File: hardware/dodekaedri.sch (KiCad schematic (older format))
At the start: 0 parts

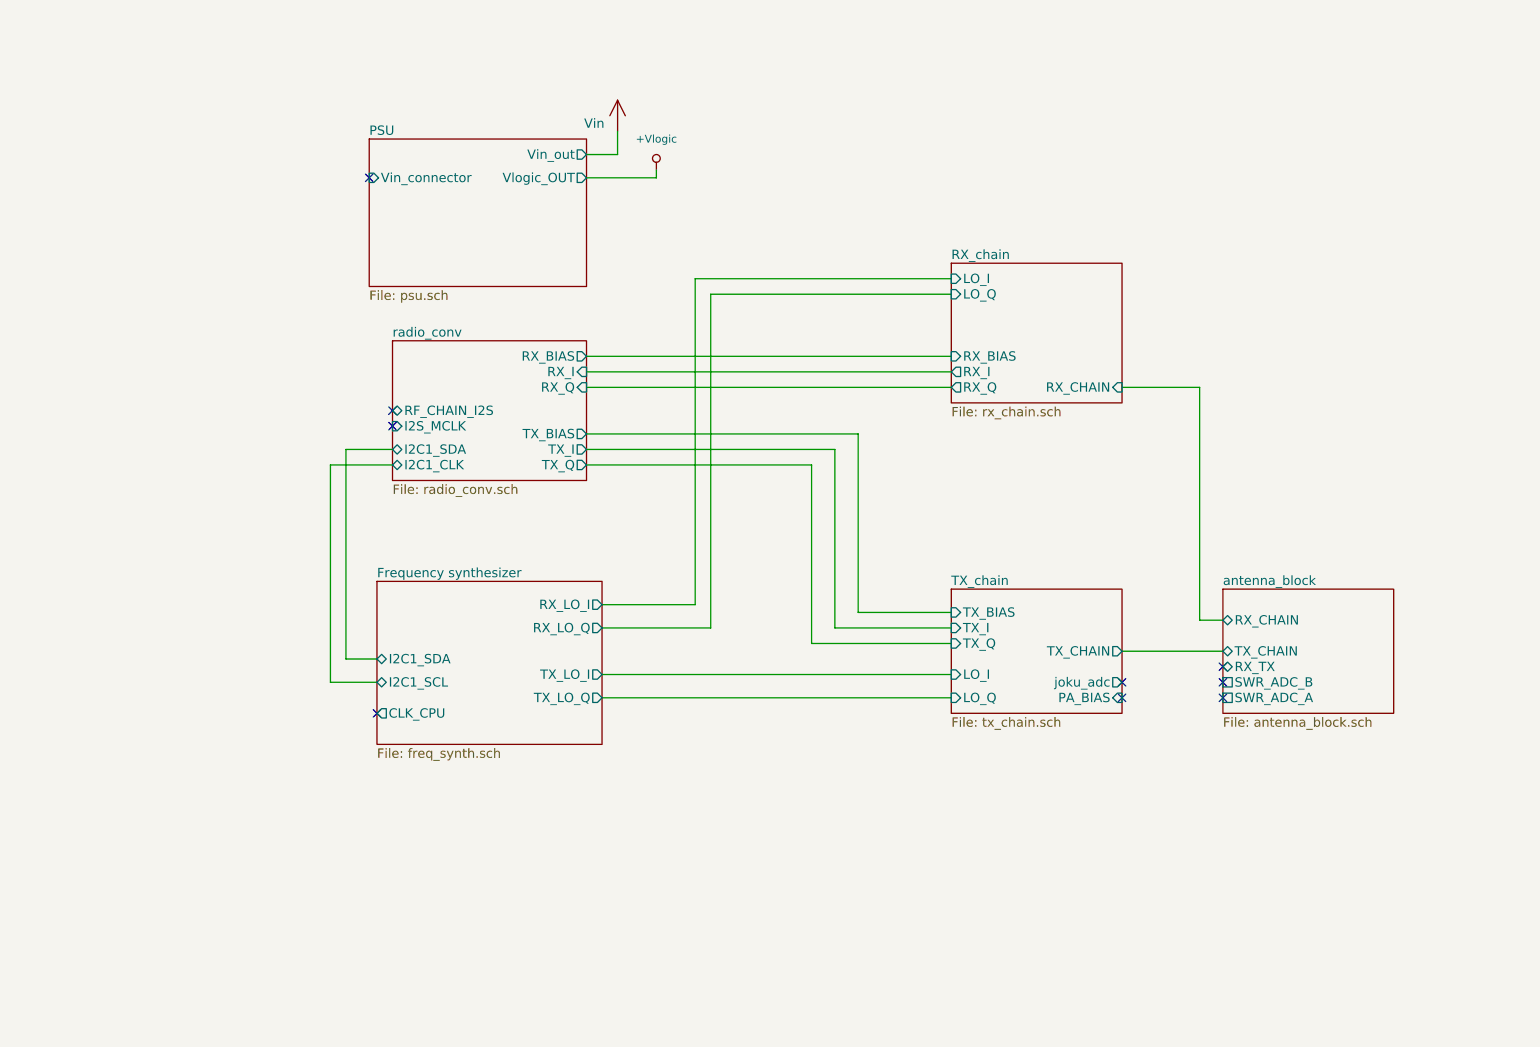
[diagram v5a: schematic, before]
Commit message: Added initial CPU block and fixed bugs from other sheets
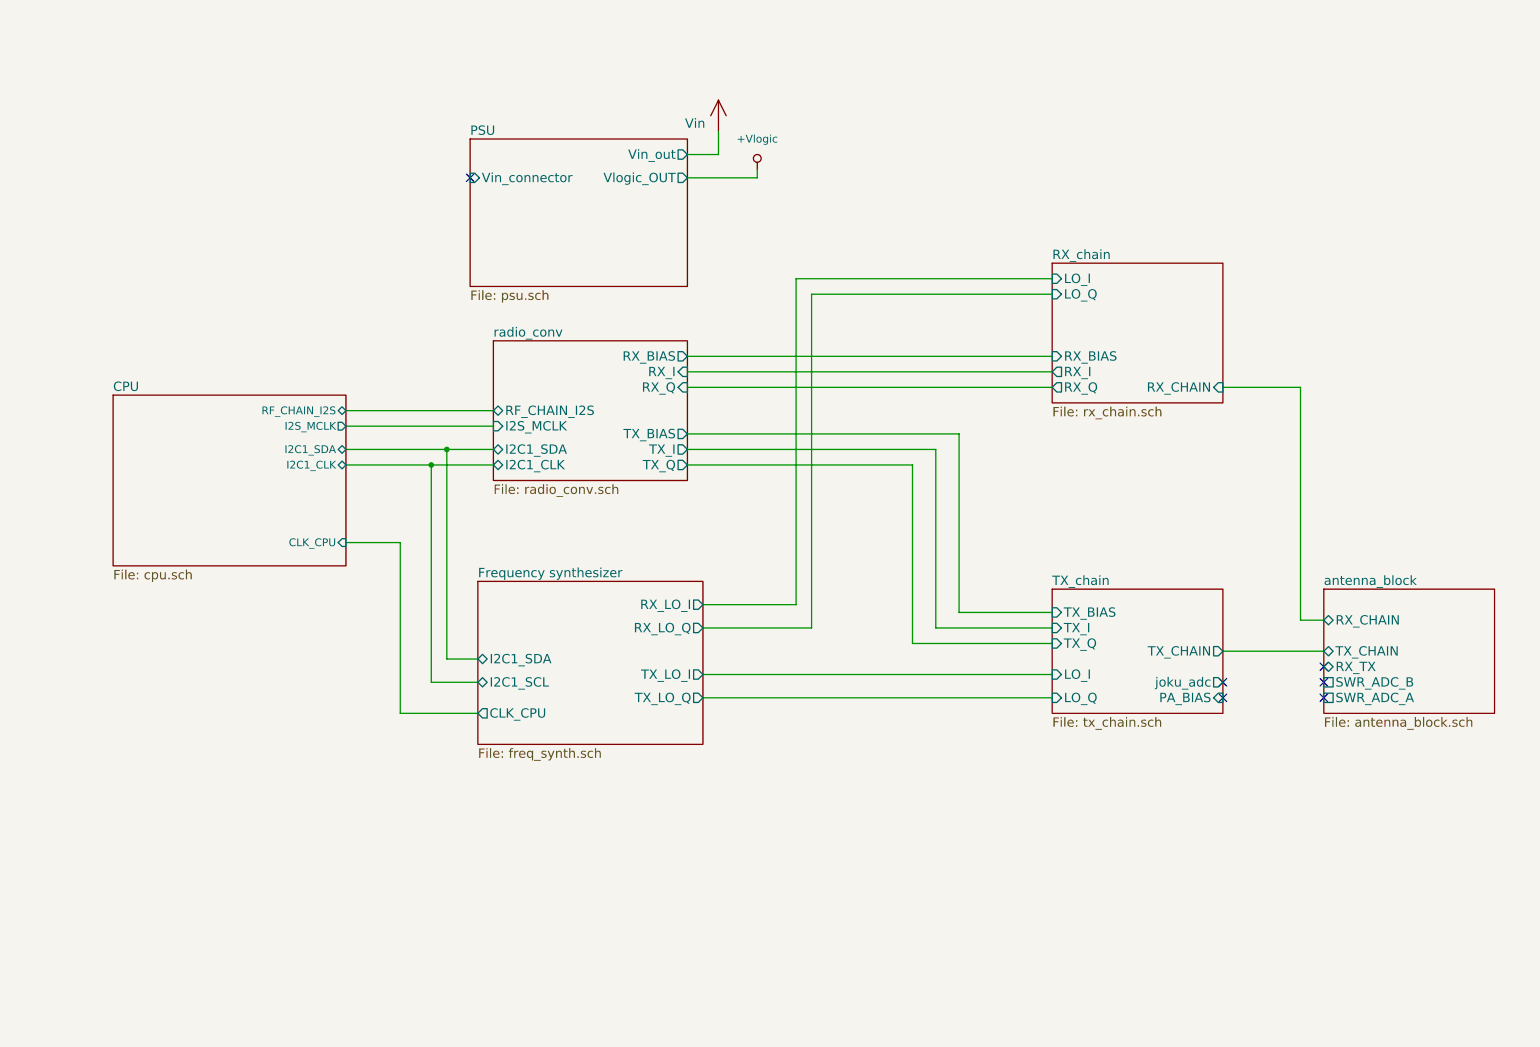
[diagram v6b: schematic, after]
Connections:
- no-connect marks 9 -> 6
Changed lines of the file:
@@
 LIBS:dodekaedri
 LIBS:Oscillators
+LIBS:stm32
 LIBS:dodekaedri-cache
 EELAYER 25 0
@@
 $Descr A4 11693 8268
 encoding utf-8
-Sheet 1 7
+Sheet 1 8
 Title "Block layer"
 Date "2016-09-20"
-Rev "0.1"
+Rev "0.4"
 Comp "PRK - OH2TI"
 Comment1 "exla - OH2EHK"
@@
 $EndDescr
 $Sheet
-S 3200 4550 1450 1050
+S 3850 4550 1450 1050
 U 57E30E5C
 F0 "Frequency synthesizer" 60
 F1 "freq_synth.sch" 60
-F2 "CLK_CPU" O L 3200 5400 60
-F3 "I2C1_SCL" B L 3200 5200 60
-F4 "I2C1_SDA" B L 3200 5050 60
-F5 "TX_LO_I" O R 4650 5150 60
-F6 "TX_LO_Q" O R 4650 5300 60
-F7 "RX_LO_Q" O R 4650 4850 60
-F8 "RX_LO_I" O R 4650 4700 60
-$EndSheet
-$Sheet
-S 8650 4600 1100 800
+F2 "CLK_CPU" O L 3850 5400 60
+F3 "I2C1_SCL" B L 3850 5200 60
+F4 "I2C1_SDA" B L 3850 5050 60
+F5 "TX_LO_I" O R 5300 5150 60
+F6 "TX_LO_Q" O R 5300 5300 60
+F7 "RX_LO_Q" O R 5300 4850 60
+F8 "RX_LO_I" O R 5300 4700 60
+$EndSheet
+$Sheet
+S 9300 4600 1100 800
 U 57E31F2A
 F0 "antenna_block" 60
 F1 "antenna_block.sch" 60
-F2 "SWR_ADC_A" U L 8650 5300 60
-F3 "SWR_ADC_B" U L 8650 5200 60
-F4 "TX_CHAIN" B L 8650 5000 60
-F5 "RX_TX" B L 8650 5100 60
-F6 "RX_CHAIN" B L 8650 4800 60
-$EndSheet
-$Sheet
-S 3150 1700 1400 950
+F2 "SWR_ADC_A" U L 9300 5300 60
+F3 "SWR_ADC_B" U L 9300 5200 60
+F4 "TX_CHAIN" B L 9300 5000 60
+F5 "RX_TX" B L 9300 5100 60
+F6 "RX_CHAIN" B L 9300 4800 60
+$EndSheet
+$Sheet
+S 3800 1700 1400 950
 U 57E31551
 F0 "PSU" 60
 F1 "psu.sch" 60
-F2 "Vlogic_OUT" O R 4550 1950 60
-F3 "Vin_connector" I L 3150 1950 60
-F4 "Vin_out" O R 4550 1800 60
+F2 "Vlogic_OUT" O R 5200 1950 60
+F3 "Vin_connector" I L 3800 1950 60
+F4 "Vin_out" O R 5200 1800 60
 $EndSheet
 $Comp
 L +Vlogic #PWR01
 U 1 1 57E3367B
-P 5000 1900
-F 0 "#PWR01" H 5000 1700 50  0001 C CNN
-F 1 "+Vlogic" H 5000 2100 50  0000 C CNN
-F 2 "" H 5000 1900 50  0000 C CNN
-F 3 "" H 5000 1900 50  0000 C CNN
-	1    5000 1900
+P 5650 1900
+F 0 "#PWR01" H 5650 1700 50  0001 C CNN
+F 1 "+Vlogic" H 5650 2100 50  0000 C CNN
+F 2 "" H 5650 1900 50  0000 C CNN
+F 3 "" H 5650 1900 50  0000 C CNN
+	1    5650 1900
 	1    0    0    -1
 $EndComp
 $Sheet
-S 6900 4600 1100 800
+S 7550 4600 1100 800
 U 57E42B3F
 F0 "TX_chain" 60
 F1 "tx_chain.sch" 60
-F2 "TX_I" I L 6900 4850 60
-F3 "TX_Q" I L 6900 4950 60
-F4 "LO_I" I L 6900 5150 60
-F5 "LO_Q" I L 6900 5300 60
-F6 "PA_BIAS" I R 8000 5300 60
-F7 "TX_CHAIN" O R 8000 5000 60
-F8 "joku_adc" O R 8000 5200 60
-F9 "TX_BIAS" I L 6900 4750 60
-$EndSheet
-NoConn ~ 3200 5400
-NoConn ~ 8000 5200
-NoConn ~ 8000 5300
-NoConn ~ 8650 5100
+F2 "TX_I" I L 7550 4850 60
+F3 "TX_Q" I L 7550 4950 60
+F4 "LO_I" I L 7550 5150 60
+F5 "LO_Q" I L 7550 5300 60
+F6 "PA_BIAS" I R 8650 5300 60
+F7 "TX_CHAIN" O R 8650 5000 60
+F8 "joku_adc" O R 8650 5200 60
+F9 "TX_BIAS" I L 7550 4750 60
+$EndSheet
 NoConn ~ 8650 5200
 NoConn ~ 8650 5300
-$Sheet
-S 6900 2500 1100 900
+NoConn ~ 9300 5100
+NoConn ~ 9300 5200
+NoConn ~ 9300 5300
+$Sheet
+S 7550 2500 1100 900
 U 57E4503B
 F0 "RX_chain" 60
 F1 "rx_chain.sch" 60
-F2 "RX_CHAIN" I R 8000 3300 60
-F3 "LO_I" I L 6900 2600 60
-F4 "LO_Q" I L 6900 2700 60
-F5 "RX_I" O L 6900 3200 60
-F6 "RX_Q" O L 6900 3300 60
-F7 "RX_BIAS" I L 6900 3100 60
-$EndSheet
-Wire Wire Line
-	4550 1950 5000 1950
-Wire Wire Line
-	5000 1950 5000 1900
-Wire Wire Line
-	6150 4850 6900 4850
-Wire Wire Line
-	6000 4950 6900 4950
-Wire Wire Line
-	4650 5150 6900 5150
-Wire Wire Line
-	4650 5300 6900 5300
-Wire Wire Line
-	8000 5000 8650 5000
-Wire Wire Line
-	4550 3800 6000 3800
-Wire Wire Line
-	6000 3800 6000 4950
-Wire Wire Line
-	6150 4850 6150 3700
-Wire Wire Line
-	6150 3700 4550 3700
-Wire Wire Line
-	3300 3700 3000 3700
-Wire Wire Line
-	3000 3700 3000 5050
-Wire Wire Line
-	3000 5050 3200 5050
-Wire Wire Line
-	3300 3800 2900 3800
-Wire Wire Line
-	2900 3800 2900 5200
-Wire Wire Line
-	2900 5200 3200 5200
-Wire Wire Line
-	5250 2600 6900 2600
-Wire Wire Line
-	5350 2700 6900 2700
-Wire Wire Line
-	8000 3300 8500 3300
-Wire Wire Line
-	8500 3300 8500 4800
-Wire Wire Line
-	8500 4800 8650 4800
-Wire Wire Line
-	4550 3200 6900 3200
-Wire Wire Line
-	4550 3300 6900 3300
-Wire Wire Line
-	4650 4700 5250 4700
-Wire Wire Line
-	5250 4700 5250 2600
-Wire Wire Line
-	5350 2700 5350 4850
-Wire Wire Line
-	5350 4850 4650 4850
-NoConn ~ 3150 1950
+F2 "RX_CHAIN" I R 8650 3300 60
+F3 "LO_I" I L 7550 2600 60
+F4 "LO_Q" I L 7550 2700 60
+F5 "RX_I" O L 7550 3200 60
+F6 "RX_Q" O L 7550 3300 60
+F7 "RX_BIAS" I L 7550 3100 60
+$EndSheet
+Wire Wire Line
+	5200 1950 5650 1950
+Wire Wire Line
+	5650 1950 5650 1900
+Wire Wire Line
+	6800 4850 7550 4850
+Wire Wire Line
+	6650 4950 7550 4950
+Wire Wire Line
+	5300 5150 7550 5150
+Wire Wire Line
+	5300 5300 7550 5300
+Wire Wire Line
+	8650 5000 9300 5000
+Wire Wire Line
+	5200 3800 6650 3800
+Wire Wire Line
+	6650 3800 6650 4950
+Wire Wire Line
+	6800 4850 6800 3700
+Wire Wire Line
+	6800 3700 5200 3700
+Wire Wire Line
+	3650 3700 3650 5050
+Wire Wire Line
+	3650 5050 3850 5050
+Wire Wire Line
+	3000 3800 3950 3800
+Wire Wire Line
+	3550 3800 3550 5200
+Wire Wire Line
+	3550 5200 3850 5200
+Wire Wire Line
+	5900 2600 7550 2600
+Wire Wire Line
+	6000 2700 7550 2700
+Wire Wire Line
+	8650 3300 9150 3300
+Wire Wire Line
+	9150 3300 9150 4800
+Wire Wire Line
+	9150 4800 9300 4800
+Wire Wire Line
+	5200 3200 7550 3200
+Wire Wire Line
+	5200 3300 7550 3300
+Wire Wire Line
+	5300 4700 5900 4700
+Wire Wire Line
+	5900 4700 5900 2600
+Wire Wire Line
+	6000 2700 6000 4850
+Wire Wire Line
+	6000 4850 5300 4850
+NoConn ~ 3800 1950
 $Comp
 L Vin #Vin?
 U 1 1 57E58C68
-P 4750 1650
-F 0 "#Vin?" H 4900 1700 60  0001 C CNN
-F 1 "Vin" H 4600 1700 60  0000 C CNN
-F 2 "" H 4750 1650 60  0001 C CNN
-F 3 "" H 4750 1650 60  0001 C CNN
-	1    4750 1650
+P 5400 1650
+F 0 "#Vin?" H 5550 1700 60  0001 C CNN
+F 1 "Vin" H 5250 1700 60  0000 C CNN
+F 2 "" H 5400 1650 60  0001 C CNN
+F 3 "" H 5400 1650 60  0001 C CNN
+	1    5400 1650
 	1    0    0    -1
 $EndComp
 Wire Wire Line
-	4550 1800 4750 1800
-Wire Wire Line
-	4750 1800 4750 1650
-NoConn ~ 3300 3450
-NoConn ~ 3300 3550
-$Sheet
-S 3300 3000 1250 900
+	5200 1800 5400 1800
+Wire Wire Line
+	5400 1800 5400 1650
+$Sheet
+S 3950 3000 1250 900
 U 57E49662
 F0 "radio_conv" 60
 F1 "radio_conv.sch" 60
-F2 "RF_CHAIN_I2S" B L 3300 3450 60
-F3 "I2C1_SDA" B L 3300 3700 60
-F4 "I2C1_CLK" B L 3300 3800 60
-F5 "I2S_MCLK" I L 3300 3550 60
-F6 "RX_I" I R 4550 3200 60
-F7 "RX_Q" I R 4550 3300 60
-F8 "TX_I" O R 4550 3700 60
-F9 "TX_Q" O R 4550 3800 60
-F10 "RX_BIAS" O R 4550 3100 60
-F11 "TX_BIAS" O R 4550 3600 60
-$EndSheet
-Wire Wire Line
-	4550 3100 6900 3100
-Wire Wire Line
-	4550 3600 6300 3600
-Wire Wire Line
-	6300 3600 6300 4750
-Wire Wire Line
-	6300 4750 6900 4750
+F2 "RF_CHAIN_I2S" B L 3950 3450 60
+F3 "I2C1_SDA" B L 3950 3700 60
+F4 "I2C1_CLK" B L 3950 3800 60
+F5 "I2S_MCLK" I L 3950 3550 60
+F6 "RX_I" I R 5200 3200 60
+F7 "RX_Q" I R 5200 3300 60
+F8 "TX_I" O R 5200 3700 60
+F9 "TX_Q" O R 5200 3800 60
+F10 "RX_BIAS" O R 5200 3100 60
+F11 "TX_BIAS" O R 5200 3600 60
+$EndSheet
+Wire Wire Line
+	5200 3100 7550 3100
+Wire Wire Line
+	5200 3600 6950 3600
+Wire Wire Line
+	6950 3600 6950 4750
+Wire Wire Line
+	6950 4750 7550 4750
+$Sheet
+S 1500 3350 1500 1100
+U 57E5C816
+F0 "CPU" 60
+F1 "cpu.sch" 60
+F2 "I2C1_SDA" B R 3000 3700 50
+F3 "I2C1_CLK" B R 3000 3800 50
+F4 "I2S_MCLK" O R 3000 3550 50
+F5 "RF_CHAIN_I2S" B R 3000 3450 50
+F6 "CLK_CPU" I R 3000 4300 50
+$EndSheet
+Connection ~ 3550 3800
+Wire Wire Line
+	3000 3700 3950 3700
+Connection ~ 3650 3700
+Wire Wire Line
+	3000 3550 3950 3550
+Wire Wire Line
+	3000 3450 3950 3450
+Wire Wire Line
+	3850 5400 3350 5400
+Wire Wire Line
+	3350 5400 3350 4300
+Wire Wire Line
+	3350 4300 3000 4300
 $EndSCHEMATC

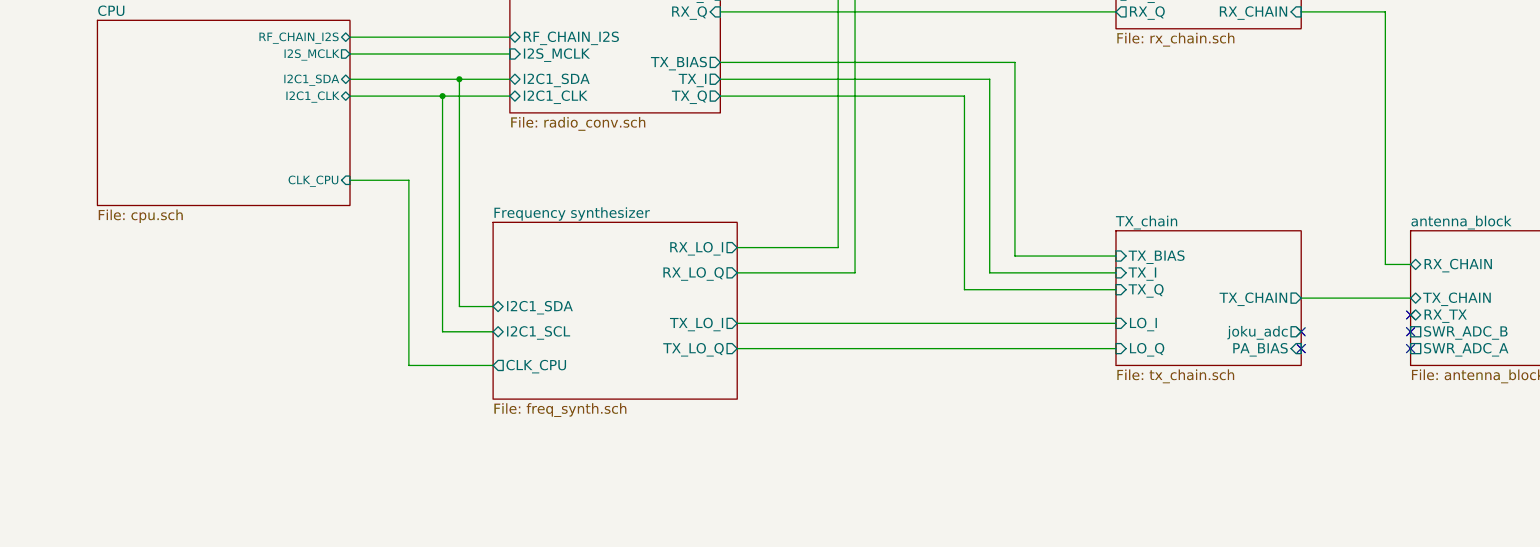
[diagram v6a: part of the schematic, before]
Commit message: Allocated CPU some pins and made minor adjustments here and there
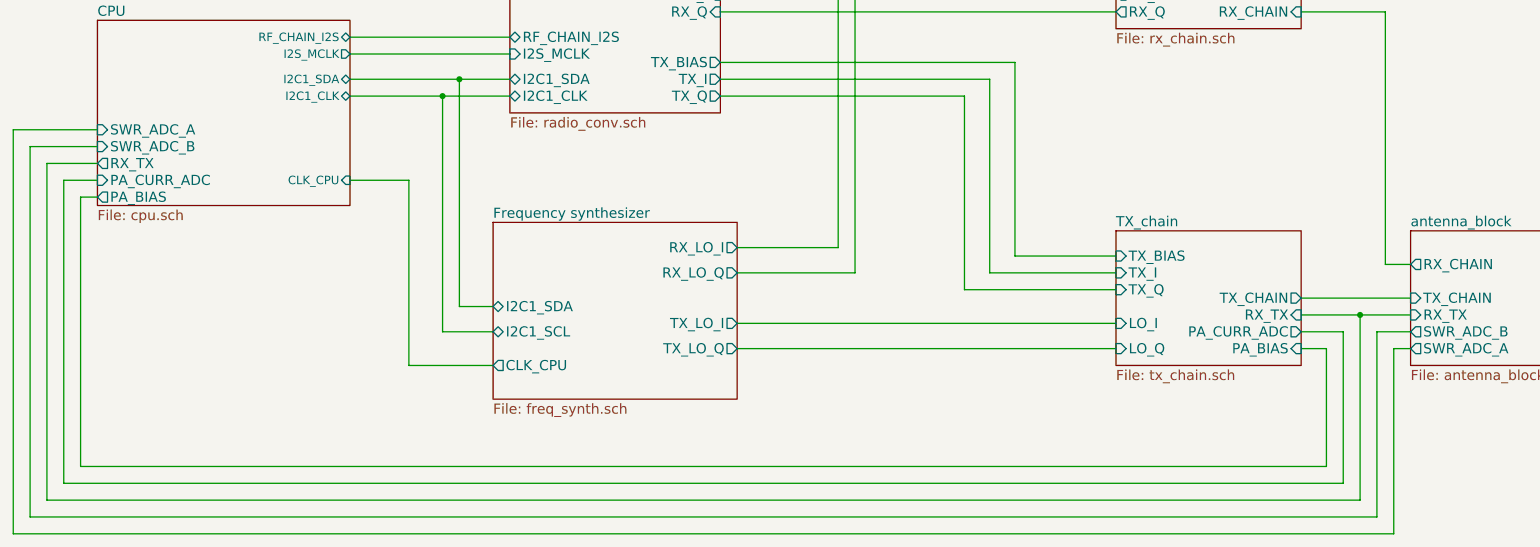
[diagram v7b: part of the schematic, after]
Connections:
- no-connect marks 6 -> 1
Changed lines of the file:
@@
 F0 "antenna_block" 60
 F1 "antenna_block.sch" 60
-F2 "SWR_ADC_A" U L 9300 5300 60
-F3 "SWR_ADC_B" U L 9300 5200 60
-F4 "TX_CHAIN" B L 9300 5000 60
-F5 "RX_TX" B L 9300 5100 60
-F6 "RX_CHAIN" B L 9300 4800 60
+F2 "SWR_ADC_A" O L 9300 5300 60
+F3 "SWR_ADC_B" O L 9300 5200 60
+F4 "TX_CHAIN" I L 9300 5000 60
+F5 "RX_TX" I L 9300 5100 60
+F6 "RX_CHAIN" O L 9300 4800 60
 $EndSheet
 $Sheet
@@
 F6 "PA_BIAS" I R 8650 5300 60
 F7 "TX_CHAIN" O R 8650 5000 60
-F8 "joku_adc" O R 8650 5200 60
-F9 "TX_BIAS" I L 7550 4750 60
-$EndSheet
-NoConn ~ 8650 5200
-NoConn ~ 8650 5300
-NoConn ~ 9300 5100
-NoConn ~ 9300 5200
-NoConn ~ 9300 5300
+F8 "TX_BIAS" I L 7550 4750 60
+F9 "PA_CURR_ADC" O R 8650 5200 60
+F10 "RX_TX" I R 8650 5100 60
+$EndSheet
 $Sheet
 S 7550 2500 1100 900
@@
 F5 "RF_CHAIN_I2S" B R 3000 3450 50
 F6 "CLK_CPU" I R 3000 4300 50
+F7 "RX_TX" O L 1500 4200 60
+F8 "SWR_ADC_A" I L 1500 4000 60
+F9 "SWR_ADC_B" I L 1500 4100 60
+F10 "PA_CURR_ADC" I L 1500 4300 60
+F11 "PA_BIAS" O L 1500 4400 60
 $EndSheet
 Connection ~ 3550 3800
@@
 Wire Wire Line
 	3350 4300 3000 4300
+Wire Wire Line
+	8650 5100 9300 5100
+Wire Wire Line
+	9000 5100 9000 6200
+Wire Wire Line
+	9000 6200 1200 6200
+Wire Wire Line
+	1200 6200 1200 4200
+Wire Wire Line
+	1200 4200 1500 4200
+Wire Wire Line
+	8650 5200 8900 5200
+Wire Wire Line
+	8900 5200 8900 6100
+Wire Wire Line
+	8900 6100 1300 6100
+Wire Wire Line
+	1300 6100 1300 4300
+Wire Wire Line
+	1300 4300 1500 4300
+Wire Wire Line
+	8650 5300 8800 5300
+Wire Wire Line
+	8800 5300 8800 6000
+Wire Wire Line
+	8800 6000 1400 6000
+Wire Wire Line
+	1400 6000 1400 4400
+Wire Wire Line
+	1400 4400 1500 4400
+Wire Wire Line
+	9300 5200 9100 5200
+Wire Wire Line
+	9100 5200 9100 6300
+Wire Wire Line
+	9100 6300 1100 6300
+Wire Wire Line
+	1100 6300 1100 4100
+Wire Wire Line
+	1100 4100 1500 4100
+Wire Wire Line
+	9300 5300 9200 5300
+Wire Wire Line
+	9200 5300 9200 6400
+Wire Wire Line
+	9200 6400 1000 6400
+Wire Wire Line
+	1000 6400 1000 4000
+Wire Wire Line
+	1000 4000 1500 4000
+Connection ~ 9000 5100
 $EndSCHEMATC
